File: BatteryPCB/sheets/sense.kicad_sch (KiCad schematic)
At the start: 3 parts

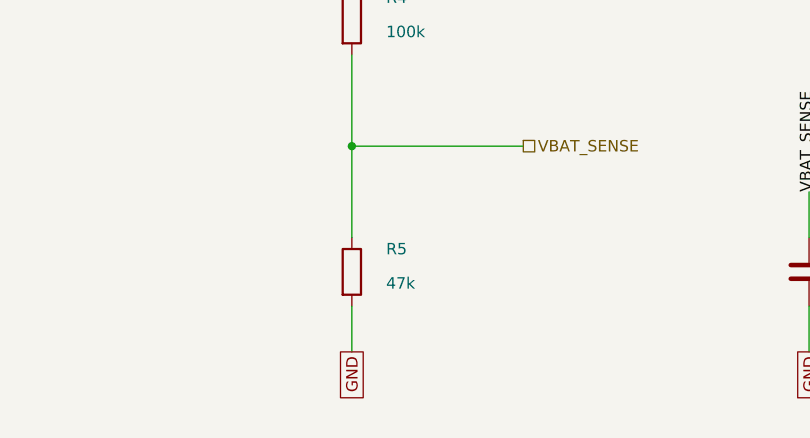
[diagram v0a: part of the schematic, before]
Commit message: Battery PCB v17: test points, strict design rules, review fixes
- Test points: TP1 +5V (buck output), TP2 VBAT+ (2S pack), TP3/TP4 GND;
  2 mm through-hole pads placed where both sides are open
- Strict rules in the project: 0.25/0.3/0.4 mm clearance (signal/power/pyro),
  0.3 mm hole clearance, 0.5 mm hole-to-hole, 0.15 mm via ring, silk spacing;
  every DRC check is an error. Fixed the spots they flagged around U1, R4, C8,
  D1/D3 silk and the TP4 label
- R5 47k -> 39k so VBAT_SENSE stays inside the ESP32 ADC range at a full pack
- BOM note: the RunCam needs a built harness (3-pin power/video + RX/TX pads)
- README: exact ESP32 to buy (ESP32-DevKitC-32E, not WROVER or 30-pin clones),
  design rules, sense scaling; layout notes for v17
- Checks: ERC 0 errors; DRC 0 violations incl. warnings with schematic parity;
  all 115 schematic pins match board pad nets; verify_A ALL PASS

Co-Authored-By: Claude Opus 5.5 <noreply@anthropic.com>
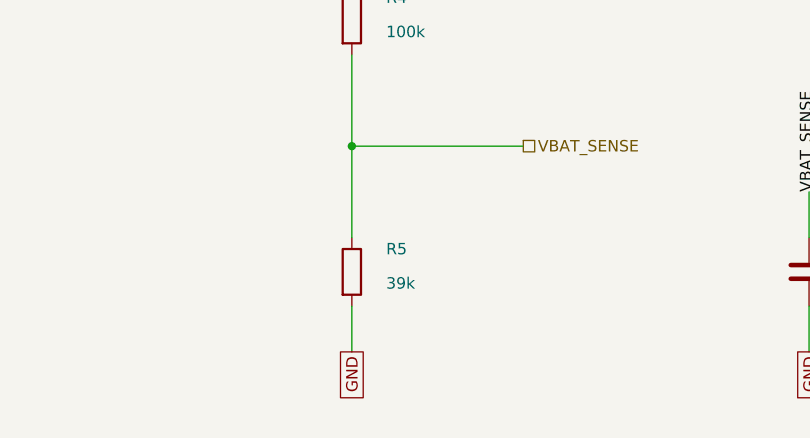
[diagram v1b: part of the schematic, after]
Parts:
- R5: value 47k -> 39k; MPN RC0603FR-0747KL -> RC0603FR-0739KL
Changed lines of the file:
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@@
 			(effects (font (size 1.27 1.27)) (justify left))
 		)
-		(property "Value" "47k"
+		(property "Value" "39k"
 			(at 63.5 78.74 0)
 			(effects (font (size 1.27 1.27)) (justify left))
@@
 			(effects (font (size 1.27 1.27)) (hide yes))
 		)
-		(property "MPN" "RC0603FR-0747KL"
+		(property "MPN" "RC0603FR-0739KL"
 			(at 59.69 77.47 0)
 			(effects (font (size 1.27 1.27)) (hide yes))

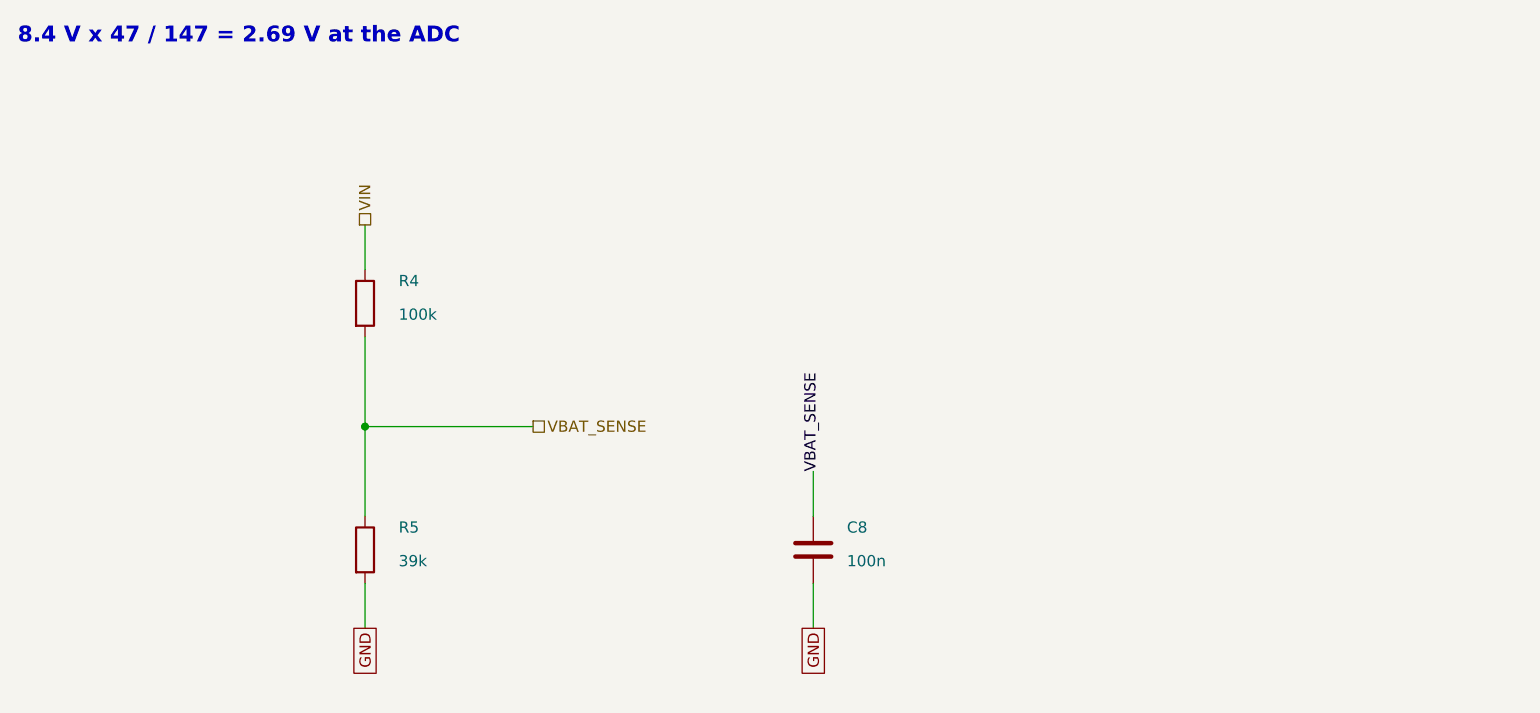
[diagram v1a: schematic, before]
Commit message: Battery PCB v19: UVLO on the buck, input caps, 6.8 uH, wired schematic
Third review (design check of the power path):
- U1 EN gets an R9/R10 divider (UVLO: on 6.3 V, off 5.5 V at VIN) so
  the 2S pack is no longer run down to 1.8 V per cell.
- Input caps per the LMR51430 datasheet: C1 is the 100 nF at U1's pins,
  C2 + new C11 (10 uF) are the bulk.
- L1 6.8 uH (TI's value for 500 kHz / 5 V out), same footprint.
- Sheets 1-3 redrawn with wires; C1/C2 moved next to U1; stale 47k
  divider note and the SS34 value on D3 corrected.
ERC 0 errors, DRC 0 (strict, schematic parity), verify_A all pass.

Co-Authored-By: Claude Opus 5.5 <noreply@anthropic.com>
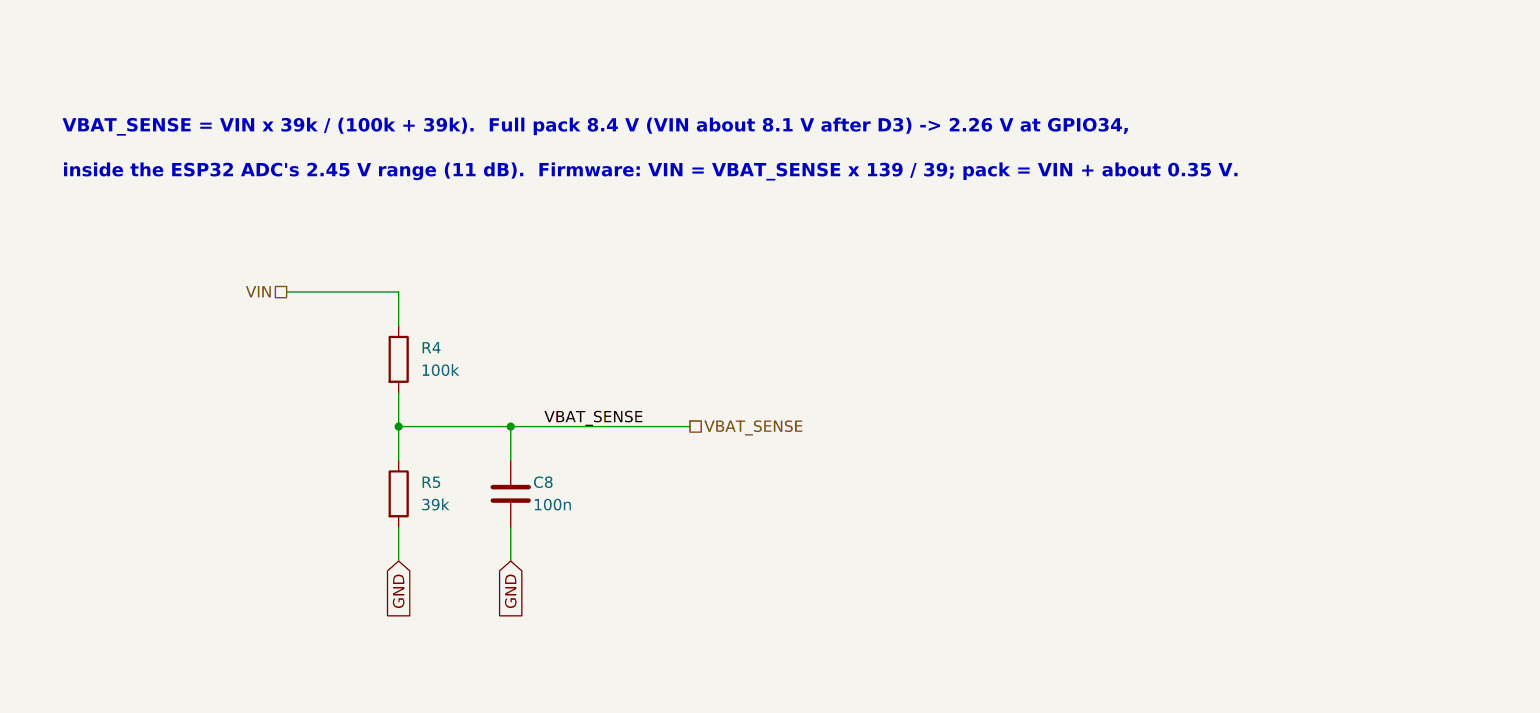
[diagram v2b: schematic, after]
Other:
- note added: "VBAT_SENSE = VIN x 39k / (100k + 39k). Full pack 8.4 V (VIN about 8.1 V after D3) -> 2.26 V at GPIO34,"
- note added: "inside the ESP32 ADC's 2.45 V range (11 dB). Firmware: VIN = VBAT_SENSE x 139 / 39; pack = VIN + about 0.35 V."
- note removed: "8.4 V x 47 / 147 = 2.69 V at the ADC"
- moved on the sheet: C8, R4, R5
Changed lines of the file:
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@@
 		(rev "A")
 	)
-	(text "8.4 V x 47 / 147 = 2.69 V at the ADC"
-		(exclude_from_sim no)
-		(at 20.32 20.32 0)
-		(effects (font (size 1.8 1.8) (bold yes)) (justify left bottom))
+	(text "VBAT_SENSE = VIN x 39k / (100k + 39k).  Full pack 8.4 V (VIN about 8.1 V after D3) -> 2.26 V at GPIO34,"
+		(exclude_from_sim no)
+		(at 25.40 30.48 0)
+		(effects (font (size 1.5 1.5) (thickness 0.254) (bold yes) (color 0 0 194 1)) (justify left bottom))
+	)
+	(text "inside the ESP32 ADC's 2.45 V range (11 dB).  Firmware: VIN = VBAT_SENSE x 139 / 39; pack = VIN + about 0.35 V."
+		(exclude_from_sim no)
+		(at 25.40 35.56 0)
+		(effects (font (size 1.5 1.5) (thickness 0.254) (bold yes) (color 0 0 194 1)) (justify left bottom))
 	)
 	(symbol
 		(lib_id "Device:R")
-		(at 59.69 49.53 0)
+		(at 63.50 55.88 0)
 		(unit 1)
 		(exclude_from_sim no)
@@
 		(fields_autoplaced yes)
 		(property "Reference" "R4"
-			(at 63.5 46.99 0)
-			(effects (font (size 1.27 1.27)) (justify left))
+			(at 66.04 54.61 0)
+			(effects (font (size 1.27 1.27)) (justify left) )
 		)
 		(property "Value" "100k"
-			(at 63.5 50.8 0)
-			(effects (font (size 1.27 1.27)) (justify left))
+			(at 66.04 57.15 0)
+			(effects (font (size 1.27 1.27)) (justify left) )
 		)
 		(property "Footprint" "Resistor_SMD:R_0603_1608Metric"
-			(at 59.69 49.53 0)
+			(at 63.50 55.88 0)
 			(effects (font (size 1.27 1.27)) (hide yes))
 		)
 		(property "Datasheet" ""
-			(at 59.69 49.53 0)
+			(at 63.50 55.88 0)
 			(effects (font (size 1.27 1.27)) (hide yes))
 		)
 		(property "Manufacturer" "Yageo"
-			(at 59.69 49.53 0)
+			(at 63.50 55.88 0)
 			(effects (font (size 1.27 1.27)) (hide yes))
 		)
 		(property "MPN" "RC0603FR-07100KL"
-			(at 59.69 49.53 0)
+			(at 63.50 55.88 0)
 			(effects (font (size 1.27 1.27)) (hide yes))
 		)
@@
 	(symbol
 		(lib_id "Device:R")
-		(at 59.69 77.47 0)
+		(at 63.50 71.12 0)
 		(unit 1)
 		(exclude_from_sim no)
@@
 		(fields_autoplaced yes)
 		(property "Reference" "R5"
-			(at 63.5 74.93 0)
-			(effects (font (size 1.27 1.27)) (justify left))
+			(at 66.04 69.85 0)
+			(effects (font (size 1.27 1.27)) (justify left) )
 		)
 		(property "Value" "39k"
-			(at 63.5 78.74 0)
-			(effects (font (size 1.27 1.27)) (justify left))
+			(at 66.04 72.39 0)
+			(effects (font (size 1.27 1.27)) (justify left) )
 		)
 		(property "Footprint" "Resistor_SMD:R_0603_1608Metric"
-			(at 59.69 77.47 0)
+			(at 63.50 71.12 0)
 			(effects (font (size 1.27 1.27)) (hide yes))
 		)
 		(property "Datasheet" ""
-			(at 59.69 77.47 0)
+			(at 63.50 71.12 0)
 			(effects (font (size 1.27 1.27)) (hide yes))
 		)
 		(property "Manufacturer" "Yageo"
-			(at 59.69 77.47 0)
+			(at 63.50 71.12 0)
 			(effects (font (size 1.27 1.27)) (hide yes))
 		)
 		(property "MPN" "RC0603FR-0739KL"
-			(at 59.69 77.47 0)
+			(at 63.50 71.12 0)
 			(effects (font (size 1.27 1.27)) (hide yes))
 		)
@@
 		)
 	)
-	(wire
-		(pts (xy 59.69 53.34) (xy 59.69 73.66))
-		(stroke (width 0) (type default))
-	)
-	(wire
-		(pts (xy 59.69 45.72) (xy 59.69 40.64))
-		(stroke (width 0) (type default))
-	)
-	(hierarchical_label "VIN"
-		(shape passive)
-		(at 59.69 40.64 90)
-		(fields_autoplaced yes)
-		(effects (font (size 1.27 1.27)) (justify left))
-	)
-	(wire
-		(pts (xy 59.69 81.28) (xy 59.69 86.36))
-		(stroke (width 0) (type default))
-	)
-	(global_label "GND"
-		(at 59.69 86.36 270)
-		(fields_autoplaced yes)
-		(effects (font (size 1.27 1.27)) (justify right))
-	)
-	(junction (at 59.69 63.5) (diameter 0) (color 0 0 0 0))
-	(wire
-		(pts (xy 59.69 63.5) (xy 78.74 63.5))
-		(stroke (width 0) (type default))
-	)
-	(hierarchical_label "VBAT_SENSE"
-		(shape passive)
-		(at 78.74 63.5 0)
-		(fields_autoplaced yes)
-		(effects (font (size 1.27 1.27)) (justify left))
-	)
 	(symbol
 		(lib_id "Device:C")
-		(at 110.49 77.47 0)
+		(at 76.20 71.12 0)
 		(unit 1)
 		(exclude_from_sim no)
@@
 		(fields_autoplaced yes)
 		(property "Reference" "C8"
-			(at 114.3 74.93 0)
-			(effects (font (size 1.27 1.27)) (justify left))
+			(at 78.74 69.85 0)
+			(effects (font (size 1.27 1.27)) (justify left) )
 		)
 		(property "Value" "100n"
-			(at 114.3 78.74 0)
-			(effects (font (size 1.27 1.27)) (justify left))
+			(at 78.74 72.39 0)
+			(effects (font (size 1.27 1.27)) (justify left) )
 		)
 		(property "Footprint" "Capacitor_SMD:C_0603_1608Metric"
-			(at 110.49 77.47 0)
+			(at 76.20 71.12 0)
 			(effects (font (size 1.27 1.27)) (hide yes))
 		)
 		(property "Datasheet" ""
-			(at 110.49 77.47 0)
+			(at 76.20 71.12 0)
 			(effects (font (size 1.27 1.27)) (hide yes))
 		)
 		(property "Manufacturer" "Samsung Electro-Mechanics"
-			(at 110.49 77.47 0)
+			(at 76.20 71.12 0)
 			(effects (font (size 1.27 1.27)) (hide yes))
 		)
 		(property "MPN" "CL10B104KB8NNNC"
-			(at 110.49 77.47 0)
+			(at 76.20 71.12 0)
 			(effects (font (size 1.27 1.27)) (hide yes))
 		)
@@
 		)
 	)
-	(wire
-		(pts (xy 110.49 73.66) (xy 110.49 68.58))
+	(hierarchical_label "VIN"
+		(shape passive)
+		(at 50.80 48.26 180)
+		(fields_autoplaced yes)
+		(effects (font (size 1.27 1.27)) (justify right))
+	)
+	(wire
+		(pts (xy 50.80 48.26) (xy 63.50 48.26))
+		(stroke (width 0) (type default))
+	)
+	(wire
+		(pts (xy 63.50 48.26) (xy 63.50 52.07))
+		(stroke (width 0) (type default))
+	)
+	(wire
+		(pts (xy 63.50 59.69) (xy 63.50 63.50))
+		(stroke (width 0) (type default))
+	)
+	(wire
+		(pts (xy 63.50 63.50) (xy 63.50 67.31))
+		(stroke (width 0) (type default))
+	)
+	(junction
+		(at 63.50 63.50)
+		(diameter 0)
+		(color 0 0 0 0)
+	)
+	(wire
+		(pts (xy 63.50 63.50) (xy 76.20 63.50))
+		(stroke (width 0) (type default))
+	)
+	(wire
+		(pts (xy 76.20 63.50) (xy 96.52 63.50))
+		(stroke (width 0) (type default))
+	)
+	(junction
+		(at 76.20 63.50)
+		(diameter 0)
+		(color 0 0 0 0)
+	)
+	(wire
+		(pts (xy 76.20 63.50) (xy 76.20 67.31))
 		(stroke (width 0) (type default))
 	)
 	(label "VBAT_SENSE"
-		(at 110.49 68.58 90)
+		(at 80.01 63.50 0)
+		(fields_autoplaced yes)
+		(effects (font (size 1.27 1.27)) (justify left bottom))
+	)
+	(hierarchical_label "VBAT_SENSE"
+		(shape passive)
+		(at 96.52 63.50 0)
 		(fields_autoplaced yes)
 		(effects (font (size 1.27 1.27)) (justify left))
 	)
 	(wire
-		(pts (xy 110.49 81.28) (xy 110.49 86.36))
+		(pts (xy 63.50 74.93) (xy 63.50 78.74))
 		(stroke (width 0) (type default))
 	)
 	(global_label "GND"
-		(at 110.49 86.36 270)
+		(shape input)
+		(at 63.50 78.74 270)
 		(fields_autoplaced yes)
 		(effects (font (size 1.27 1.27)) (justify right))
+		(property "Intersheetrefs" "${INTERSHEET_REFS}"
+			(at 63.50 78.74 0)
+			(effects (font (size 1.27 1.27)) (hide yes))
+		)
+	)
+	(wire
+		(pts (xy 76.20 74.93) (xy 76.20 78.74))
+		(stroke (width 0) (type default))
+	)
+	(global_label "GND"
+		(shape input)
+		(at 76.20 78.74 270)
+		(fields_autoplaced yes)
+		(effects (font (size 1.27 1.27)) (justify right))
+		(property "Intersheetrefs" "${INTERSHEET_REFS}"
+			(at 76.20 78.74 0)
+			(effects (font (size 1.27 1.27)) (hide yes))
+		)
 	)
 )
